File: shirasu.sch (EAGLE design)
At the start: 122 parts, among them J1 XT60PW-F, J2 XT60PW-M, J3 EP2.5-4-SIDE, J4 EP2.5-4-SIDE, J5 RJHSE-5381-02, J6 10118192-0001LF, Q1 TPH1R405PL,L1Q, Q2 TPH1R405PL,L1Q, Q3 TPH1R405PL,L1Q, Q4 TPH1R405PL,L1Q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

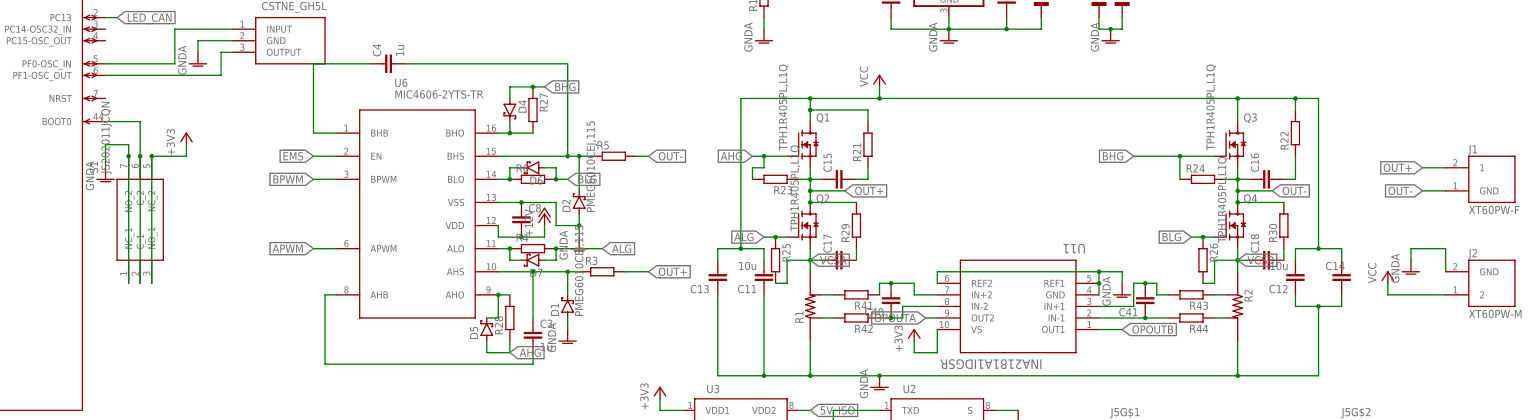
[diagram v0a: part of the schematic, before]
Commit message: fixed xt connector removed some resistors and capacitors
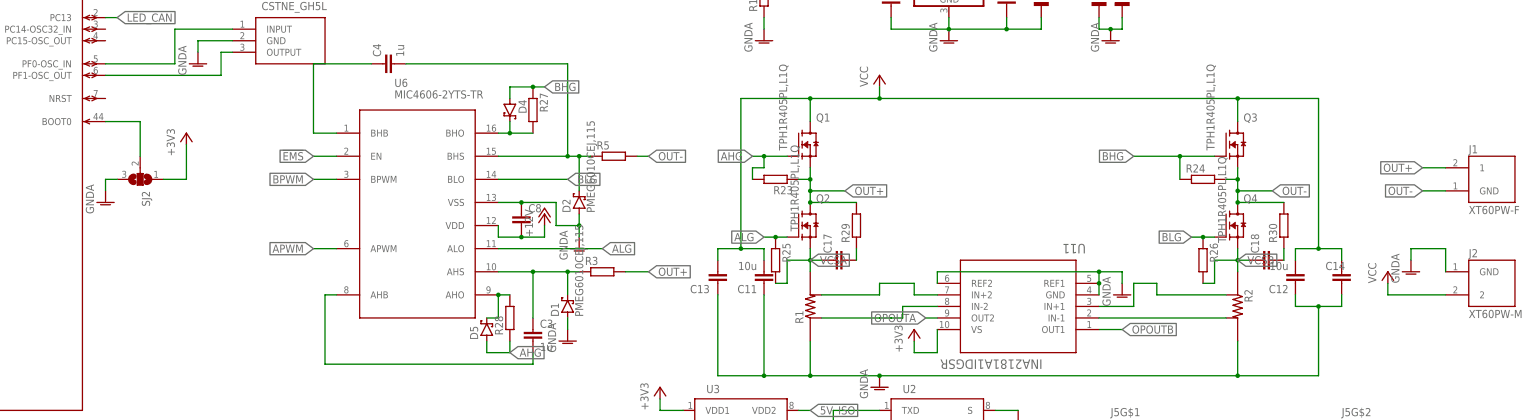
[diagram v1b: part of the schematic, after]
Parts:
- removed C15, C16, C40, C41: (no value), rcl:C-EUC0603
- removed D6, D7: PMEG6010CEJ,115, nexperia:PMEG6010CEJ,115
- removed R21, R22, R4, R41, R42, R43, R44, R6: (no value), rcl:R-EU_R0603
- removed S1: JS202011JCQN, switch-slide:JS202011JCQN
- added SJ2: (no value), jumper:SJ2W
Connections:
- removed net N$29: C15.2, R21.1
- removed net N$31: C16.2, R22.1
- removed net N$45: C40.2, R41.1, U11.IN+2
- removed net N$46: C40.1, R42.1, U11.IN-2
- removed net N$53: C41.1, R44.2, U11.IN-1
- removed net N$54: C41.2, R43.2, U11.IN+1
- removed net N$6: D6.C, R6.1, U6.BLO
- removed net N$7: D7.C, R4.1, U6.ALO
- net +3V3: now also SJ2.1; no longer S1.NC_2, S1.NO_1
- net ALG: now also U6.ALO; no longer D7.A, R4.2
- net BLG: now also U6.BLO; no longer D6.A, R6.2
- net GNDA: now also SJ2.3; no longer S1.NC_1, S1.NO_2
- net N$48: now also U11.IN+2; no longer R41.2
- net N$49: now also SJ2.2; no longer S1.C_1, S1.C_2
- net N$50: now also U11.IN-2; no longer R42.2
- net N$51: now also U11.IN+1; no longer R43.1
- net N$52: now also U11.IN-1; no longer R44.1
- net OUT+: no longer C15.1
- net OUT-: no longer C16.1
- net VCC: no longer R21.2, R22.2

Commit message: ver1.0
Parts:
- removed C13, C14, C24, C25, C26, C27: (no value), rcl:C-EUC0603
- removed C36: (no value), rcl:CPOL-EUE2.5-5
- removed R13, R14, R17, R20, R23, R24, R25, R26, R33, R34, R35, R36: (no value), rcl:R-EU_R0603
- removed R32: 4k7, rcl:R-EU_R0603
- removed R45: 10k, rcl:R-EU_R0603
- removed U7: 7812DT, linear:7812DT
- removed U8: 7805DT, linear:7805DT
- added C15: 2.2u, rcl:C-EUC0603
- added C16, C23: 100n, rcl:C-EUC0603
- added IC1: 78L12F, linear:78L12F
- added IC2: 78L05F, linear:78L05F
- added R4: 100, rcl:R-EU_R0603
- added R6: 180, rcl:R-EU_R0603
- added RT1: NCP15XH103F03RC, NCP15XH103F03RC:NCP15XH103F03RC
- C10, C30, C31, C32, C33, C5, C7: value (none) -> 100n
- C17, C18: value (none) -> 470n
- C19, C20, C38, C39, C8: value (none) -> 1u
- C21: value (none) -> 100n; device rcl:CPOL-EUE2.5-5 -> rcl:C-EUC0603
- C34: value 100n -> 10n
- C37, C9: value (none) -> 330n
- C6: value (none) -> 470p
- R10: value 4k7 -> 3.3k
- R11: value 4k7 -> 0.68; device rcl:R-EU_R0603 -> rcl:R-EU_R1206
- R12: value (none) -> 180
- R15, R39: value (none) -> 10k
- R16: value (none) -> 470
- R18: value (none) -> 3.6k
- R19, R7, R8, R9: value (none) -> 1.2k
- R27, R28: value (none) -> 40
- R29, R30: value (none) -> 2
- R3, R5: value (none) -> 3
- R37, R38: value (none) -> 10
- R40: value (none) -> 1k
- renumbered U6 to U$1
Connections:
- net N$49 renamed BOOT0
- removed net N$18: J5G$2.A-G, R11.2
- removed net N$20: J5G$1.A-G, R10.2
- removed net N$21: J5G$2.A-Y, R13.2
- removed net N$37: D8.2, J6.VUSB, R32.2
- removed net N$38: J3.4, R34.1
- removed net N$40: J3.3, R33.1
- removed net N$43: J4.3, R35.1
- removed net N$44: J4.4, R36.1
- removed net N$48: R1.4, U11.IN+2
- removed net N$50: R1.3, U11.IN-2
- removed net N$51: R2.3, U11.IN+1
- removed net N$52: R2.4, U11.IN-1
- new net N$29: R2.4, U11.IN-2
- new net N$31: R1.3, U11.IN-1
- new net N$6: J5G$2.A-G, R4.2
- new net N$7: J5G$1.A-G, J5G$2.C-G
- new net TEMP: C15.2, R10.2, RT1.1, U1A.PA4
- net !EMS: no longer R17.2
- net +12V: now also IC1.VO; no longer C21.+, U7.VO
- net +3V3: now also C23.1, R31.1, RT1.2
- net 5V_ISO: now also C21.2, IC2.VO, R4.1; no longer R10.1, R11.1, U8.VO
- net AHG: no longer R23.2
- net ALG: no longer R25.1
- net APWM: now also U1A.PA2; no longer U1A.PB14
- net BHG: no longer R24.1
- net BLG: no longer R26.1
- net BPWM: now also U1A.PA3; no longer U1A.PB15
- net DIN_A: now also J4.3, U1A.PA8; no longer C27.2, R35.2, U1A.PB6
- net DIN_B: now also J4.4, U1A.PA10; no longer C26.2, R36.2, U1A.PB5
- net ENC_A: now also J3.3; no longer C25.2, R33.2
- net ENC_B: now also J3.4; no longer C24.2, R34.2
- net GNDA: now also C15.1, C23.2, IC1.GND, IC1.GND@1, R10.1, U$1.NC; no longer C13.2, C14.2, C21.-, C24.1, C25.1, C26.1, C27.1, R17.1, R45.2, U7.GND
- net GNDIO: now also C16.2, C21.1, IC2.GND, IC2.GND@1; no longer C36.-, J5G$2.C-G, U8.GND
- net ISENSEA: now also U1A.PA7; no longer U1A.PA4
- net ISENSEB: now also U1A.PA1; no longer U1A.PA0
- net LED_CAN: now also R6.2, U1A.PB4; no longer R13.1, U1A.PC13
- net LED_GREEN: now also U1A.PB12; no longer U1A.PB1
- net LED_RED: now also U1A.PB14; no longer U1A.PB13
- net LED_YELLOW: now also U1A.PB13; no longer U1A.PB12
- net N$12: now also J5G$1.A-Y, R6.1; no longer R31.1, U1A.PA10
- net N$13: now also J5G$2.A-Y, R12.2; no longer R32.1, R45.1, U1A.PA8
- net N$17: now also U5.G; no longer R14.2
- net N$19: now also C16.1, IC2.VI; no longer C36.+, U8.VI
- net N$22: now also R1.4, U11.IN+1; no longer J5G$1.A-Y, R12.2
- net N$23: now also R2.3, U11.IN+2; no longer R14.1, U5.G
- net N$30: now also R11.2; no longer R20.1
- net OUT+: no longer R23.1
- net OUT-: no longer R24.2
- net VCC: now also IC1.VI, R11.1; no longer C13.1, C14.1, R20.2, U7.VI
- net VCSA: no longer R25.2
- net VCSB: no longer R26.2
- net VSENSE: now also U1A.PA0; no longer U1A.PB11
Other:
- moved on the sheet: C11, C12, R10, R11, R12, R31, U11, U3

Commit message: use TIM1 for pwm instead of TIM15,add gate resistors for low side MOSFET as well.
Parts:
- removed F1: (no value), rcl:R-EU_R1206
- added C13, C14: 6800p, rcl:C-EUC0603
- added C24: (no value), rcl:CPOL-EUE2.5-5
- added D6, D7: PMEG6010CEJ,115, nexperia:PMEG6010CEJ,115
- added R13, R14, R17, R20: 2, rcl:R-EU_R0603
- C17, C18: value 470n -> 6800p
- R27: value 40 -> 2
- renumbered IC1 to U7, IC2 to U8, SJ2 to BOOT0, U$1 to U6
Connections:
- new net N$18: C14.2, R14.1
- new net N$20: C13.2, R13.1
- new net N$21: D7.C, R20.1, U6.ALO
- net !EMS: now also U1A.PB11; no longer U1A.PA9
- net ALG: now also D7.A, R20.2; no longer U6.ALO
- net APWM: now also U1A.PA9; no longer U1A.PA2
- net BLG: now also D6.A, R17.2; no longer U6.BLO
- net BPWM: now also U1A.PA8; no longer U1A.PA3
- net DIN_A: now also U1A.PB6; no longer U1A.PA8
- net GNDIO: now also C24.-
- net ISENSEA: now also U1A.PB0
- net ISENSEB: now also U1A.PA3, U1A.PA4; no longer U1A.PA1
- net N$15: now also C16.1, C24.+, U8.VI; no longer F1.2
- net N$19: now also D6.C, R17.1, U6.BLO; no longer C16.1, F1.1, U8.VI
- net OUT+: now also C13.1
- net OUT-: now also C14.1
- net TEMP: now also U1A.PA1; no longer U1A.PA4
- net VCC: now also R13.2, R14.2

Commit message: BOMを追加
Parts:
- C1, C2: value (none) -> 220u
- C15: value 2.2u -> 1u
- C22, C24: value (none) -> 47u
- C38, C39: value 1u -> 330p
- C6: value 470p -> 100p
- LED1: value (none) -> RED
- LED2: value (none) -> YELLOW
- LED3: value (none) -> GREEN
- R1, R2: value (none) -> 1m
- R28: value 40 -> 2
- R3, R5: value 3 -> 2
- R37, R38: value 10 -> 1k

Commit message: ver1.2
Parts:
- R39: value 10k -> 1k
- R40: value 1k -> 10k
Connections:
- net GNDA: now also R39.1; no longer R40.1
- net ISENSEB: now also U1A.PA5; no longer U1A.PA4
- net VCC: now also R40.2; no longer R39.2
- net VSENSE: now also R39.2, R40.1; no longer R39.1, R40.2
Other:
- moved on the sheet: R39, R40
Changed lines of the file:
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@@
 <part name="+3V4" library="supply1" library_urn="urn:adsk.eagle:library:371" deviceset="+3V3" device=""/>
 <part name="P+12" library="supply1" library_urn="urn:adsk.eagle:library:371" deviceset="VCC" device=""/>
-<part name="R39" library="rcl" library_urn="urn:adsk.eagle:library:334" deviceset="R-EU_" device="R0603" package3d_urn="urn:adsk.eagle:package:23555/3" value="10k"/>
-<part name="R40" library="rcl" library_urn="urn:adsk.eagle:library:334" deviceset="R-EU_" device="R0603" package3d_urn="urn:adsk.eagle:package:23555/3" value="1k"/>
+<part name="R40" library="rcl" library_urn="urn:adsk.eagle:library:334" deviceset="R-EU_" device="R0603" package3d_urn="urn:adsk.eagle:package:23555/3" value="10k"/>
+<part name="R39" library="rcl" library_urn="urn:adsk.eagle:library:334" deviceset="R-EU_" device="R0603" package3d_urn="urn:adsk.eagle:package:23555/3" value="1k"/>
 <part name="GND38" library="supply1" library_urn="urn:adsk.eagle:library:371" deviceset="GNDA" device=""/>
 <part name="C30" library="rcl" library_urn="urn:adsk.eagle:library:334" deviceset="C-EU" device="C0603" package3d_urn="urn:adsk.eagle:package:23616/2" value="100n"/>
@@
 <attribute name="VALUE" x="-22.86" y="22.86" size="1.778" layer="96" rot="R90"/>
 </instance>
-<instance part="R39" gate="G$1" x="-20.32" y="15.24" smashed="yes" rot="R90">
+<instance part="R40" gate="G$1" x="-20.32" y="15.24" smashed="yes" rot="R90">
 <attribute name="NAME" x="-21.8186" y="13.97" size="1.778" layer="95" rot="R90"/>
 <attribute name="VALUE" x="-17.018" y="11.43" size="1.778" layer="96" rot="R90"/>
 </instance>
-<instance part="R40" gate="G$1" x="-20.32" y="0" smashed="yes" rot="R90">
+<instance part="R39" gate="G$1" x="-20.32" y="0" smashed="yes" rot="R90">
 <attribute name="NAME" x="-21.8186" y="-1.27" size="1.778" layer="95" rot="R90"/>
 <attribute name="VALUE" x="-17.018" y="-3.81" size="1.778" layer="96" rot="R90"/>
@@
 </segment>
 <segment>
-<pinref part="R40" gate="G$1" pin="1"/>
+<pinref part="R39" gate="G$1" pin="1"/>
 <pinref part="GND38" gate="1" pin="GNDA"/>
 <wire x1="-20.32" y1="-5.08" x2="-20.32" y2="-7.62" width="0.1524" layer="91"/>
@@
 </segment>
 <segment>
-<pinref part="R39" gate="G$1" pin="2"/>
+<pinref part="R40" gate="G$1" pin="2"/>
 <pinref part="P+12" gate="VCC" pin="VCC"/>
 <wire x1="-20.32" y1="20.32" x2="-20.32" y2="22.86" width="0.1524" layer="91"/>
@@
 <net name="VSENSE" class="0">
 <segment>
-<pinref part="R39" gate="G$1" pin="1"/>
-<pinref part="R40" gate="G$1" pin="2"/>
+<pinref part="R40" gate="G$1" pin="1"/>
+<pinref part="R39" gate="G$1" pin="2"/>
 <wire x1="-20.32" y1="10.16" x2="-20.32" y2="7.62" width="0.1524" layer="91"/>
 <wire x1="-20.32" y1="7.62" x2="-20.32" y2="5.08" width="0.1524" layer="91"/>
@@
 <junction x="25.4" y="88.9"/>
 <label x="48.26" y="76.2" size="1.778" layer="95" rot="R180"/>
-<pinref part="U1" gate="A" pin="PA4"/>
-<wire x1="60.96" y1="73.66" x2="55.88" y2="73.66" width="0.1524" layer="91"/>
 <wire x1="55.88" y1="73.66" x2="38.1" y2="73.66" width="0.1524" layer="91"/>
 <wire x1="38.1" y1="73.66" x2="38.1" y2="88.9" width="0.1524" layer="91"/>
@@
 <wire x1="60.96" y1="76.2" x2="55.88" y2="76.2" width="0.1524" layer="91"/>
 <wire x1="55.88" y1="76.2" x2="55.88" y2="73.66" width="0.1524" layer="91"/>
+<pinref part="U1" gate="A" pin="PA5"/>
+<wire x1="60.96" y1="71.12" x2="55.88" y2="71.12" width="0.1524" layer="91"/>
+<wire x1="55.88" y1="71.12" x2="55.88" y2="73.66" width="0.1524" layer="91"/>
 <junction x="55.88" y="73.66"/>
 </segment>
